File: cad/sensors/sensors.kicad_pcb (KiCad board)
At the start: 2 copper layers, 72 x 50 mm, 80 parts, among them J1 Conn_01x04, J2 Conn_01x04, J3 6P6C, J4 Conn_01x04, J5 Conn_01x04, J6 Conn_01x04, J7 Conn_01x02, U1 LMV324, U2 PCA9517A, U3 LMV331, U4 MC14040B, U5 MC14040B, U6 TCA9555DBR, U7 PCF8574

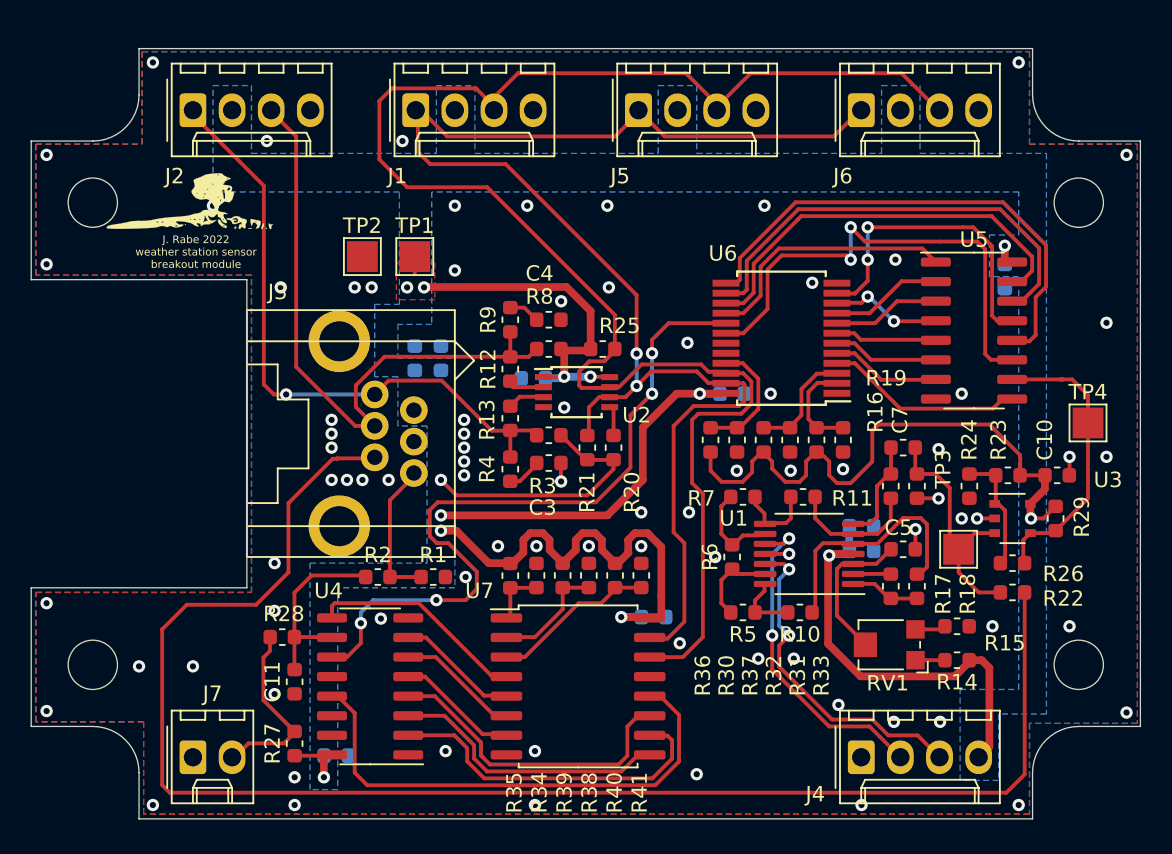
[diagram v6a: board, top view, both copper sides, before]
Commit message: Finished PCB layout
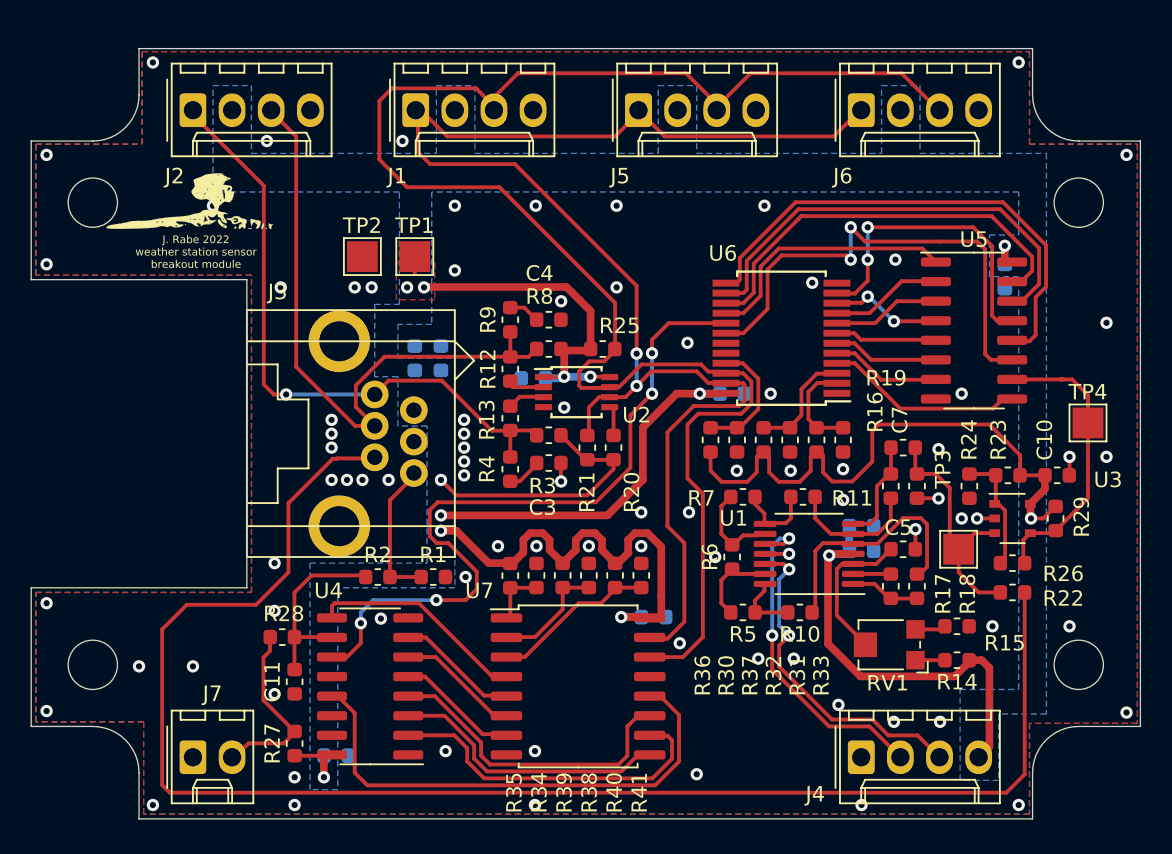
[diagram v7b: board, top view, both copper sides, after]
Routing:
- net /SCL: track 107.7 -> 108.5 mm
- net /SDA: track 94.1 -> 94.7 mm
- net GND: vias 80 -> 83
- net (no net): vias 3 -> 1
